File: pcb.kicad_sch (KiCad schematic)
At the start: 16 parts, among them IC1 BQ25606RGER, J1 PTHF-126-02-GF-Q-368, J1 Screw_Terminal_01x05, J2 Screw_Terminal_01x05, J3 Conn_01x01_Male

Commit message: added MPPT & STM32
added spv1040t mppt circuit and stm32f405 chip with its bare minimum components and labelling required pinouts.
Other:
- added sheet MPPTv2 (MPPTv2.kicad_sch)
- added sheet STM32F405board (STM32F405board.kicad_sch)
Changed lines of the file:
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@@
     (pin "1")
     (instances
-      (project ""
-        (path "/f47b3abd-889a-4280-a952-2080b48a2756"
+      (project "pcb"
+        (path "/a8bac665-9e81-4c8d-8e7f-b88478edfeaf"
           (reference "#PWR0108") (unit 1)
         )
       )
+      (project ""
+        (path "/f47b3abd-889a-4280-a952-2080b48a2756"
+          (reference "#PWR0108") (unit 1)
+        )
+      )
     )
   )
@@
     (pin "1")
     (instances
-      (project ""
-        (path "/f47b3abd-889a-4280-a952-2080b48a2756"
+      (project "pcb"
+        (path "/a8bac665-9e81-4c8d-8e7f-b88478edfeaf"
           (reference "#PWR0104") (unit 1)
         )
       )
+      (project ""
+        (path "/f47b3abd-889a-4280-a952-2080b48a2756"
+          (reference "#PWR0104") (unit 1)
+        )
+      )
     )
   )
@@
     (pin "1")
     (instances
-      (project ""
-        (path "/f47b3abd-889a-4280-a952-2080b48a2756"
+      (project "pcb"
+        (path "/a8bac665-9e81-4c8d-8e7f-b88478edfeaf"
           (reference "#PWR0107") (unit 1)
         )
       )
+      (project ""
+        (path "/f47b3abd-889a-4280-a952-2080b48a2756"
+          (reference "#PWR0107") (unit 1)
+        )
+      )
     )
   )
@@
     (pin "1")
     (instances
-      (project ""
-        (path "/f47b3abd-889a-4280-a952-2080b48a2756"
+      (project "pcb"
+        (path "/a8bac665-9e81-4c8d-8e7f-b88478edfeaf"
           (reference "#PWR02") (unit 1)
         )
       )
+      (project ""
+        (path "/f47b3abd-889a-4280-a952-2080b48a2756"
+          (reference "#PWR02") (unit 1)
+        )
+      )
     )
   )
@@
     (pin "1")
     (instances
+      (project "pcb"
+        (path "/a8bac665-9e81-4c8d-8e7f-b88478edfeaf"
+          (reference "#PWR0109") (unit 1)
+        )
+      )
       (project ""
         (path "/f47b3abd-889a-4280-a952-2080b48a2756"
@@
     (pin "1")
     (instances
+      (project "pcb"
+        (path "/a8bac665-9e81-4c8d-8e7f-b88478edfeaf"
+          (reference "#PWR0102") (unit 1)
+        )
+      )
       (project ""
         (path "/f47b3abd-889a-4280-a952-2080b48a2756"
@@
     (pin "1")
     (instances
+      (project "pcb"
+        (path "/a8bac665-9e81-4c8d-8e7f-b88478edfeaf"
+          (reference "#PWR0106") (unit 1)
+        )
+      )
       (project ""
         (path "/f47b3abd-889a-4280-a952-2080b48a2756"
@@
     (pin "1")
     (instances
+      (project "pcb"
+        (path "/a8bac665-9e81-4c8d-8e7f-b88478edfeaf"
+          (reference "#PWR0103") (unit 1)
+        )
+      )
       (project ""
         (path "/f47b3abd-889a-4280-a952-2080b48a2756"
@@
     (pin "1")
     (instances
+      (project "pcb"
+        (path "/a8bac665-9e81-4c8d-8e7f-b88478edfeaf"
+          (reference "#PWR01") (unit 1)
+        )
+      )
       (project ""
         (path "/f47b3abd-889a-4280-a952-2080b48a2756"
@@
     (pin "1")
     (instances
+      (project "pcb"
+        (path "/a8bac665-9e81-4c8d-8e7f-b88478edfeaf"
+          (reference "#PWR0101") (unit 1)
+        )
+      )
       (project ""
         (path "/f47b3abd-889a-4280-a952-2080b48a2756"
@@
     (pin "1")
     (instances
+      (project "pcb"
+        (path "/a8bac665-9e81-4c8d-8e7f-b88478edfeaf"
+          (reference "#PWR0105") (unit 1)
+        )
+      )
       (project ""
         (path "/f47b3abd-889a-4280-a952-2080b48a2756"
@@
       )
     )
+  )
+  (sheet (at 76.2 20.32) (size 34.29 20.32) (fields_autoplaced)
+    (stroke (width 0.1524) (type solid))
+    (fill (color 0 0 0 0.0000))
+    (property "Sheetname" "STM32F405board" (at 76.2 19.6084 0)
+      (effects (font (size 1.27 1.27)) (justify left bottom))
+    )
+    (property "Sheetfile" "STM32F405board.kicad_sch" (at 76.2 41.2246 0)
+      (effects (font (size 1.27 1.27)) (justify left top))
+    )
+    (instances
+      (project "pcb"
+        (path "/a8bac665-9e81-4c8d-8e7f-b88478edfeaf" (page "3"))
+      )
+    )
+  )
+  (sheet (at 31.75 19.05) (size 33.02 21.59) (fields_autoplaced)
+    (stroke (width 0.1524) (type solid))
+    (fill (color 0 0 0 0.0000))
+    (property "Sheetname" "MPPTv2" (at 31.75 18.3384 0)
+      (effects (font (size 1.27 1.27)) (justify left bottom))
+    )
+    (property "Sheetfile" "MPPTv2.kicad_sch" (at 31.75 41.2246 0)
+      (effects (font (size 1.27 1.27)) (justify left top))
+    )
+    (instances
+      (project "pcb"
+        (path "/a8bac665-9e81-4c8d-8e7f-b88478edfeaf" (page "2"))
+      )
+    )

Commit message: Added protection circuit
added protection citcuit with tps25961 ic for 3.3V and 5V bus.
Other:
- added sheet ProtectionCircuit (ProtectionCircuit.kicad_sch)
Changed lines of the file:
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@@
+    )
+  )
+  (sheet (at 118.11 20.32) (size 38.1 21.59) (fields_autoplaced)
+    (stroke (width 0.1524) (type solid))
+    (fill (color 0 0 0 0.0000))
+    (property "Sheetname" "ProtectionCircuit" (at 118.11 19.6084 0)
+      (effects (font (size 1.27 1.27)) (justify left bottom))
+    )
+    (property "Sheetfile" "ProtectionCircuit.kicad_sch" (at 118.11 42.4946 0)
+      (effects (font (size 1.27 1.27)) (justify left top))
+    )
+    (instances
+      (project "pcb"
+        (path "/a8bac665-9e81-4c8d-8e7f-b88478edfeaf" (page "4"))
+      )
     )
   )

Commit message: Major
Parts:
- removed C1: 1uF, 1uF cap:C1206, symbol Device:C
- removed C2: 4.7uF, cap 4.7uf:C1210, symbol Device:C
- removed C3: 47nF, 47nF:C1005_Commercial, symbol Device:C
- removed C4, C5: 10uF, 10uF MLCC:CAPC2012X94N, symbol Device:C
- removed IC1: BQ25606RGER, QFN50P400X400X100-25N-D, symbol BQ25606RGER:BQ25606RGER
- removed J1, J2: Screw_Terminal_01x05, TerminalBlock_MetzConnect:TerminalBlock_MetzConnect_Type059_RT06305HBWC_1x05_P3.50mm_Horizontal, symbol Connector:Screw_Terminal_01x05
- removed J3: Conn_01x01_Male, Connector_PinHeader_1.00mm:PinHeader_1x01_P1.00mm_Vertical, symbol Connector:Conn_01x01_Male
- removed L1: 1uH, 1uH indc:IHHP0805ZHER1R0M01, symbol Device:L
- removed R1, R2: 2.2k, 2.2k rst:RESC2012X65N, symbol Device:R
- removed R3: 330, rst 330:H2C_H2R, symbol Device:R
- removed R4: 10k, 10k rst:ERA8KEB1004V, symbol Device:R
- removed R5: 430, rst 430:ERJH3, symbol Device:R
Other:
- added sheet Battery Charger (battch.kicad_sch)
- added sheet Regulation Module (regulate.kicad_sch)

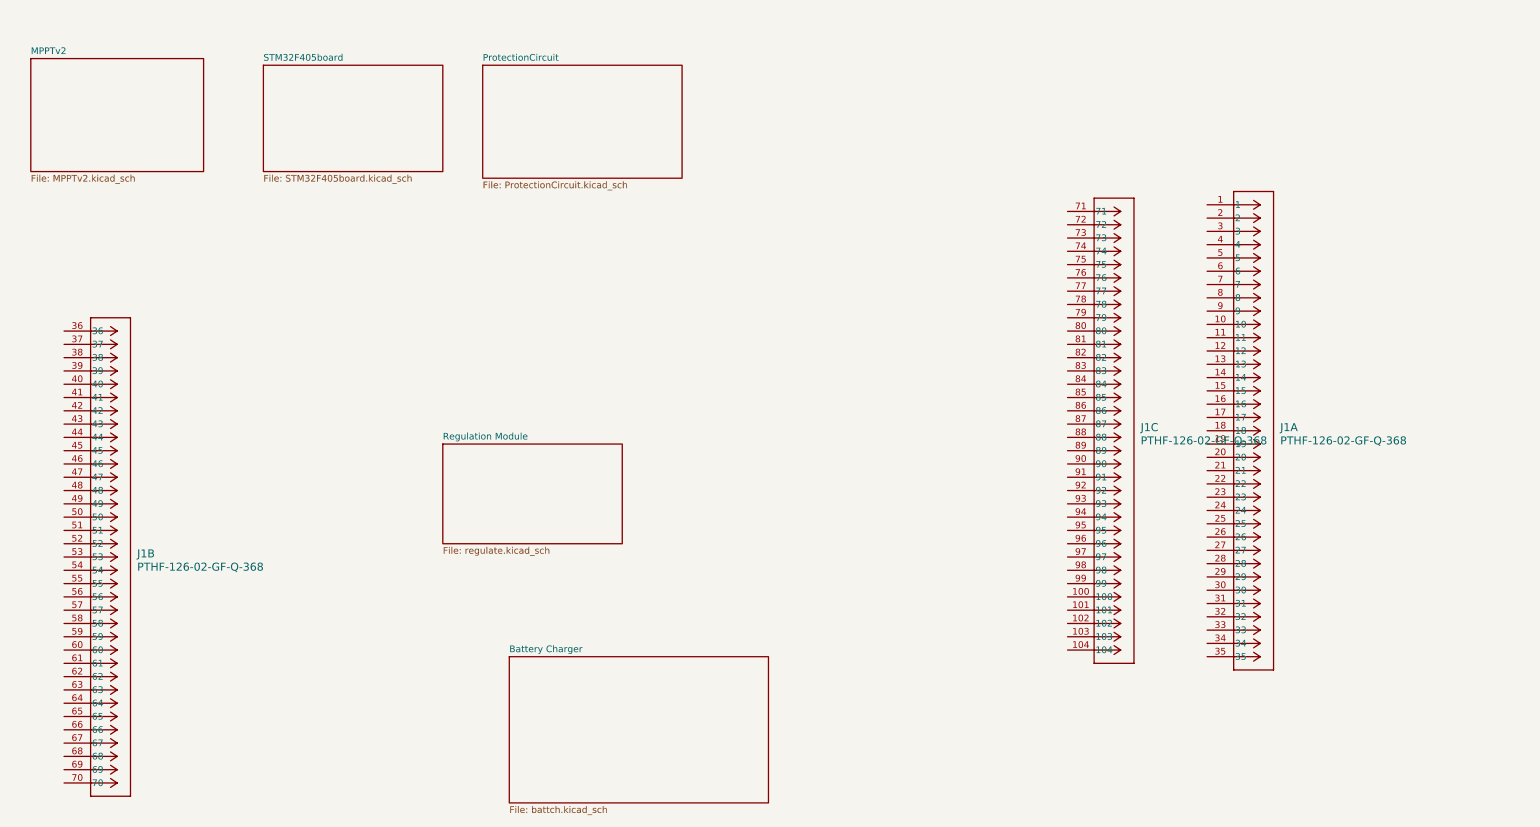
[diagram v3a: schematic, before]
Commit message: Final Schematic
Final Schematic. PC104 pins not assigned.
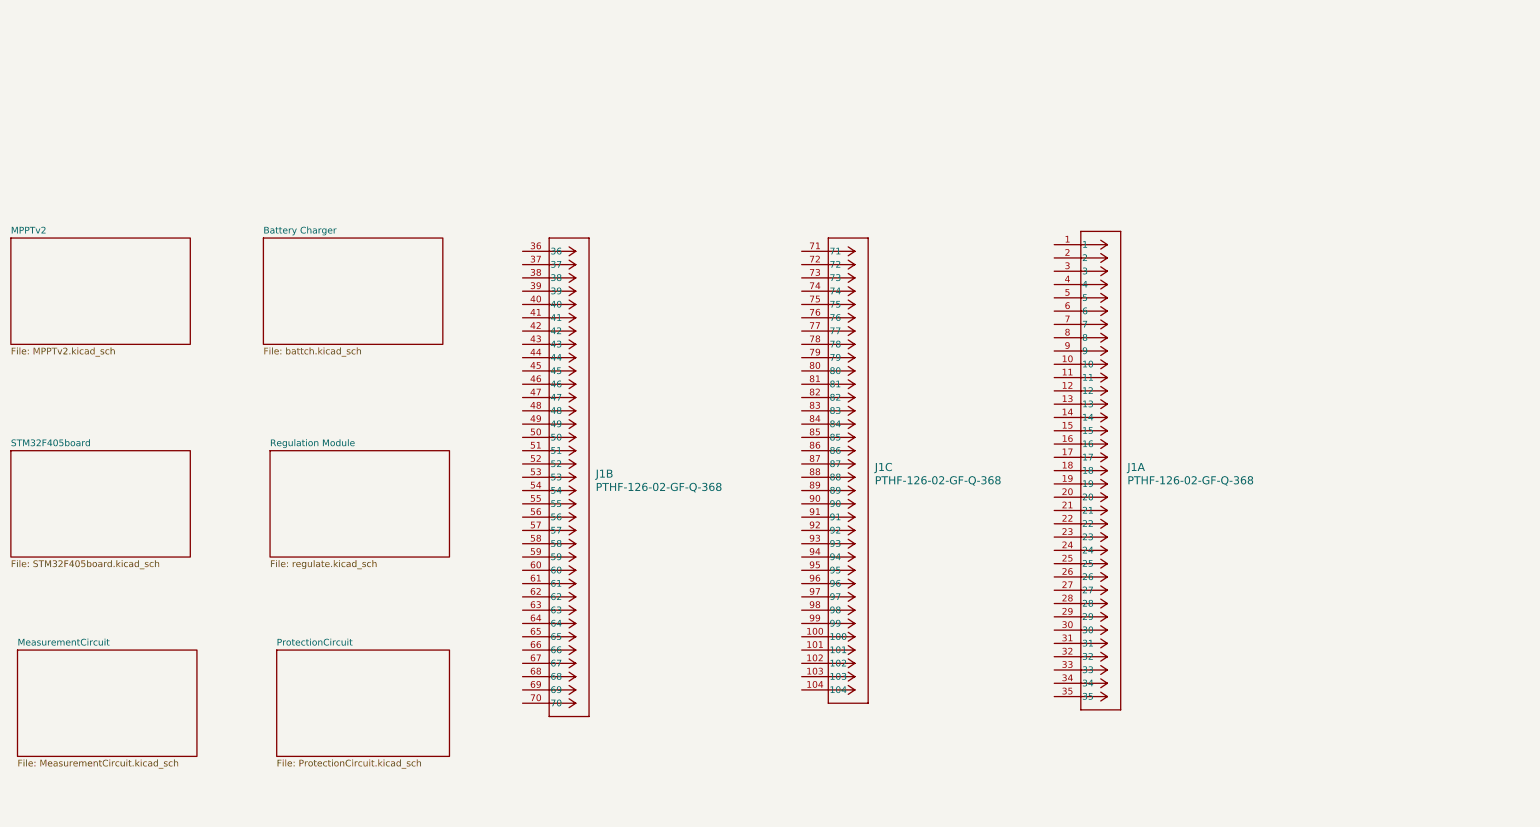
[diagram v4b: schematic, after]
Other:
- added sheet MeasurementCircuit (MeasurementCircuit.kicad_sch)
- moved on the sheet: J1A, J1B, J1C
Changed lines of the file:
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@@
 (kicad_sch (version 20230121) (generator eeschema)
   (paper "A4")
-  (symbol (lib_id "PC104 conn:PTHF-126-02-GF-Q-368") (at 256.54 46.99 0) (unit 1)
+  (symbol (lib_id "PC104 conn:PTHF-126-02-GF-Q-368") (at 227.33 54.61 0) (unit 1)
     (in_bom yes) (on_board yes) (dnp no) (fields_autoplaced)
-    (property "Reference" "J1" (at 270.51 89.535 0)
-      (effects (font (size 1.524 1.524)) (justify left))
-    )
-    (property "Value" "PTHF-126-02-GF-Q-368" (at 270.51 92.075 0)
-      (effects (font (size 1.524 1.524)) (justify left))
-    )
-    (property "Footprint" "CONN_PTHF-126-02-GF-Q-368_SAI" (at 256.54 46.99 0)
-      (effects (font (size 1.27 1.27) italic) hide)
-    )
-    (property "Datasheet" "PTHF-126-02-GF-Q-368" (at 256.54 46.99 0)
+    (property "Reference" "J1" (at 241.3 97.155 0)
+      (effects (font (size 1.524 1.524)) (justify left))
+    )
+    (property "Value" "PTHF-126-02-GF-Q-368" (at 241.3 99.695 0)
+      (effects (font (size 1.524 1.524)) (justify left))
+    )
+    (property "Footprint" "CONN_PTHF-126-02-GF-Q-368_SAI" (at 227.33 54.61 0)
+      (effects (font (size 1.27 1.27) italic) hide)
+    )
+    (property "Datasheet" "PTHF-126-02-GF-Q-368" (at 227.33 54.61 0)
       (effects (font (size 1.27 1.27) italic) hide)
     )
@@
     )
   )
-  (symbol (lib_id "PC104 conn:PTHF-126-02-GF-Q-368") (at 38.1 71.12 0) (unit 2)
+  (symbol (lib_id "PC104 conn:PTHF-126-02-GF-Q-368") (at 125.73 55.88 0) (unit 2)
     (in_bom yes) (on_board yes) (dnp no) (fields_autoplaced)
-    (property "Reference" "J1" (at 52.07 113.665 0)
-      (effects (font (size 1.524 1.524)) (justify left))
-    )
-    (property "Value" "PTHF-126-02-GF-Q-368" (at 52.07 116.205 0)
-      (effects (font (size 1.524 1.524)) (justify left))
-    )
-    (property "Footprint" "CONN_PTHF-126-02-GF-Q-368_SAI" (at 38.1 71.12 0)
-      (effects (font (size 1.27 1.27) italic) hide)
-    )
-    (property "Datasheet" "PTHF-126-02-GF-Q-368" (at 38.1 71.12 0)
+    (property "Reference" "J1" (at 139.7 98.425 0)
+      (effects (font (size 1.524 1.524)) (justify left))
+    )
+    (property "Value" "PTHF-126-02-GF-Q-368" (at 139.7 100.965 0)
+      (effects (font (size 1.524 1.524)) (justify left))
+    )
+    (property "Footprint" "CONN_PTHF-126-02-GF-Q-368_SAI" (at 125.73 55.88 0)
+      (effects (font (size 1.27 1.27) italic) hide)
+    )
+    (property "Datasheet" "PTHF-126-02-GF-Q-368" (at 125.73 55.88 0)
       (effects (font (size 1.27 1.27) italic) hide)
     )
@@
     )
   )
-  (symbol (lib_id "PC104 conn:PTHF-126-02-GF-Q-368") (at 229.87 48.26 0) (unit 3)
+  (symbol (lib_id "PC104 conn:PTHF-126-02-GF-Q-368") (at 179.07 55.88 0) (unit 3)
     (in_bom yes) (on_board yes) (dnp no) (fields_autoplaced)
-    (property "Reference" "J1" (at 243.84 89.535 0)
-      (effects (font (size 1.524 1.524)) (justify left))
-    )
-    (property "Value" "PTHF-126-02-GF-Q-368" (at 243.84 92.075 0)
-      (effects (font (size 1.524 1.524)) (justify left))
-    )
-    (property "Footprint" "CONN_PTHF-126-02-GF-Q-368_SAI" (at 229.87 48.26 0)
-      (effects (font (size 1.27 1.27) italic) hide)
-    )
-    (property "Datasheet" "PTHF-126-02-GF-Q-368" (at 229.87 48.26 0)
+    (property "Reference" "J1" (at 193.04 97.155 0)
+      (effects (font (size 1.524 1.524)) (justify left))
+    )
+    (property "Value" "PTHF-126-02-GF-Q-368" (at 193.04 99.695 0)
+      (effects (font (size 1.524 1.524)) (justify left))
+    )
+    (property "Footprint" "CONN_PTHF-126-02-GF-Q-368_SAI" (at 179.07 55.88 0)
+      (effects (font (size 1.27 1.27) italic) hide)
+    )
+    (property "Datasheet" "PTHF-126-02-GF-Q-368" (at 179.07 55.88 0)
       (effects (font (size 1.27 1.27) italic) hide)
     )
@@
     )
   )
-  (sheet (at 123.19 133.35) (size 49.53 27.94) (fields_autoplaced)
-    (stroke (width 0.1524) (type solid))
-    (fill (color 0 0 0 0.0000))
-    (property "Sheetname" "Battery Charger" (at 123.19 132.6384 0)
-      (effects (font (size 1.27 1.27)) (justify left bottom))
-    )
-    (property "Sheetfile" "battch.kicad_sch" (at 123.19 161.8746 0)
+  (sheet (at 76.2 53.34) (size 34.29 20.32) (fields_autoplaced)
+    (stroke (width 0.1524) (type solid))
+    (fill (color 0 0 0 0.0000))
+    (property "Sheetname" "Battery Charger" (at 76.2 52.6284 0)
+      (effects (font (size 1.27 1.27)) (justify left bottom))
+    )
+    (property "Sheetfile" "battch.kicad_sch" (at 76.2 74.2446 0)
       (effects (font (size 1.27 1.27)) (justify left top))
     )
@@
     )
   )
-  (sheet (at 76.2 20.32) (size 34.29 20.32) (fields_autoplaced)
-    (stroke (width 0.1524) (type solid))
-    (fill (color 0 0 0 0.0000))
-    (property "Sheetname" "STM32F405board" (at 76.2 19.6084 0)
-      (effects (font (size 1.27 1.27)) (justify left bottom))
-    )
-    (property "Sheetfile" "STM32F405board.kicad_sch" (at 76.2 41.2246 0)
+  (sheet (at 27.94 93.98) (size 34.29 20.32) (fields_autoplaced)
+    (stroke (width 0.1524) (type solid))
+    (fill (color 0 0 0 0.0000))
+    (property "Sheetname" "STM32F405board" (at 27.94 93.2684 0)
+      (effects (font (size 1.27 1.27)) (justify left bottom))
+    )
+    (property "Sheetfile" "STM32F405board.kicad_sch" (at 27.94 114.8846 0)
       (effects (font (size 1.27 1.27)) (justify left top))
     )
@@
     )
   )
-  (sheet (at 110.49 92.71) (size 34.29 19.05) (fields_autoplaced)
-    (stroke (width 0.1524) (type solid))
-    (fill (color 0 0 0 0.0000))
-    (property "Sheetname" "Regulation Module" (at 110.49 91.9984 0)
-      (effects (font (size 1.27 1.27)) (justify left bottom))
-    )
-    (property "Sheetfile" "regulate.kicad_sch" (at 110.49 112.3446 0)
+  (sheet (at 77.47 93.98) (size 34.29 20.32) (fields_autoplaced)
+    (stroke (width 0.1524) (type solid))
+    (fill (color 0 0 0 0.0000))
+    (property "Sheetname" "Regulation Module" (at 77.47 93.2684 0)
+      (effects (font (size 1.27 1.27)) (justify left bottom))
+    )
+    (property "Sheetfile" "regulate.kicad_sch" (at 77.47 114.8846 0)
       (effects (font (size 1.27 1.27)) (justify left top))
     )
@@
     )
   )
-  (sheet (at 118.11 20.32) (size 38.1 21.59) (fields_autoplaced)
-    (stroke (width 0.1524) (type solid))
-    (fill (color 0 0 0 0.0000))
-    (property "Sheetname" "ProtectionCircuit" (at 118.11 19.6084 0)
-      (effects (font (size 1.27 1.27)) (justify left bottom))
-    )
-    (property "Sheetfile" "ProtectionCircuit.kicad_sch" (at 118.11 42.4946 0)
+  (sheet (at 78.74 132.08) (size 33.02 20.32) (fields_autoplaced)
+    (stroke (width 0.1524) (type solid))
+    (fill (color 0 0 0 0.0000))
+    (property "Sheetname" "ProtectionCircuit" (at 78.74 131.3684 0)
+      (effects (font (size 1.27 1.27)) (justify left bottom))
+    )
+    (property "Sheetfile" "ProtectionCircuit.kicad_sch" (at 78.74 152.9846 0)
       (effects (font (size 1.27 1.27)) (justify left top))
     )
@@
     )
   )
-  (sheet (at 31.75 19.05) (size 33.02 21.59) (fields_autoplaced)
-    (stroke (width 0.1524) (type solid))
-    (fill (color 0 0 0 0.0000))
-    (property "Sheetname" "MPPTv2" (at 31.75 18.3384 0)
-      (effects (font (size 1.27 1.27)) (justify left bottom))
-    )
-    (property "Sheetfile" "MPPTv2.kicad_sch" (at 31.75 41.2246 0)
-      (effects (font (size 1.27 1.27)) (justify left top))
-    )
+  (sheet (at 29.21 132.08) (size 34.29 20.32) (fields_autoplaced)
+    (stroke (width 0.1524) (type solid))
+    (fill (color 0 0 0 0.0000))
+    (property "Sheetname" "MeasurementCircuit" (at 29.21 131.3684 0)
+      (effects (font (size 1.27 1.27)) (justify left bottom))
+    )
+    (property "Sheetfile" "MeasurementCircuit.kicad_sch" (at 29.21 152.9846 0)
+      (effects (font (size 1.27 1.27)) (justify left top))
+    )
+    (instances
+      (project "pcb"
+        (path "/a8bac665-9e81-4c8d-8e7f-b88478edfeaf" (page "7"))
+      )
+    )
+  )
+  (sheet (at 27.94 53.34) (size 34.29 20.32) (fields_autoplaced)
+    (stroke (width 0.1524) (type solid))
+    (fill (color 0 0 0 0.0000))
+    (property "Sheetname" "MPPTv2" (at 27.94 52.6284 0)
+      (effects (font (size 1.27 1.27)) (justify left bottom))
+    )
+    (property "Sheetfile" "MPPTv2.kicad_sch" (at 27.94 74.2446 0)
+      (effects (font (size 1.27 1.27)) (justify left top))
+    )
